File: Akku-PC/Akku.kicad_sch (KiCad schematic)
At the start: 59 parts, among them J1 Conn_02x10_Odd_Even, J2 Conn_01x02, J3 Conn_01x04, J4 Conn_01x02, J5 Conn_02x10_Odd_Even, J6 Conn_02x10_Odd_Even, J7 Conn_01x02, J8 Conn_01x02, SW1 Digitast, SW2 Digitast, SW3 Digitast, U1 74HC14, U2 74HC00, U4 74HC08, U5 74LS193, U6 74LS541, U7 74LS193, U8 74LS540

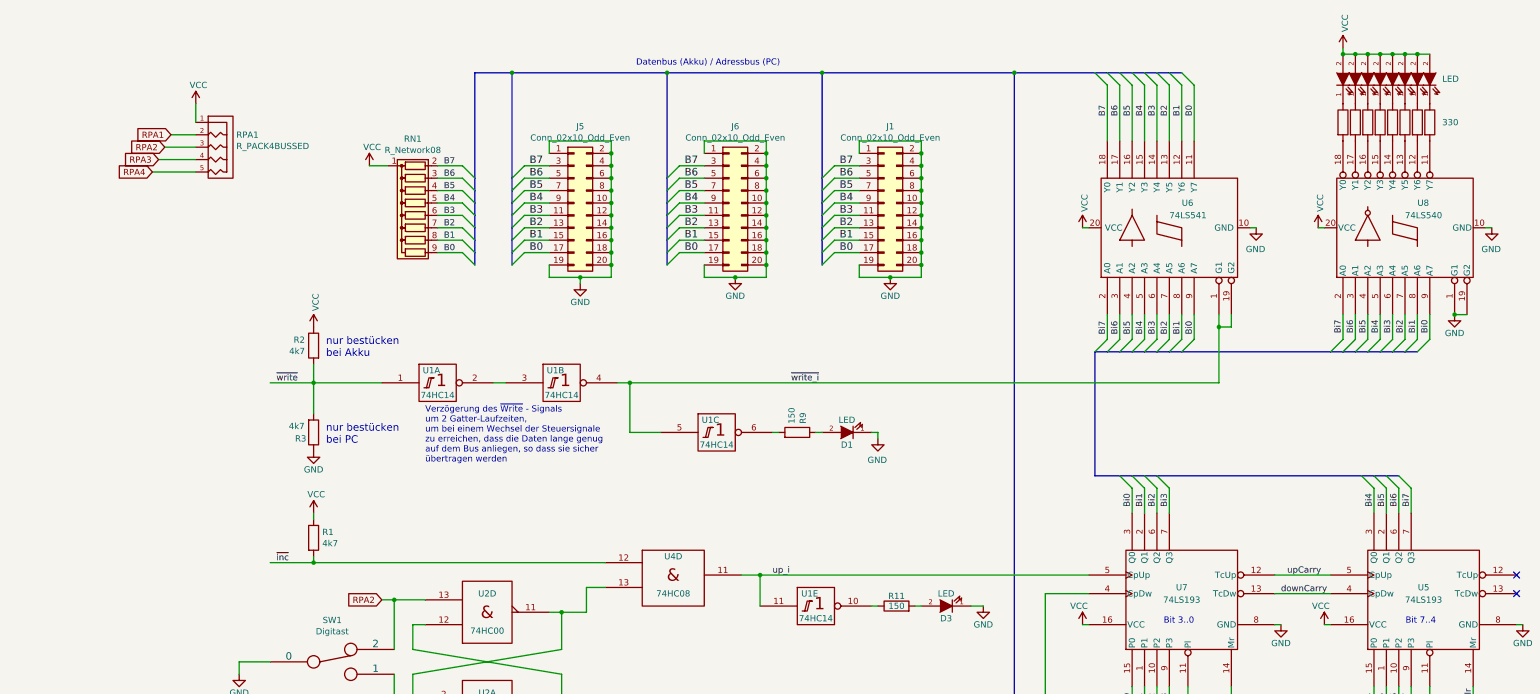
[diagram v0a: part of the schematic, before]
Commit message: - Werte von Bauteilen in den Schaltplänen ergänzt - weitere Hinweise zum Nachbau
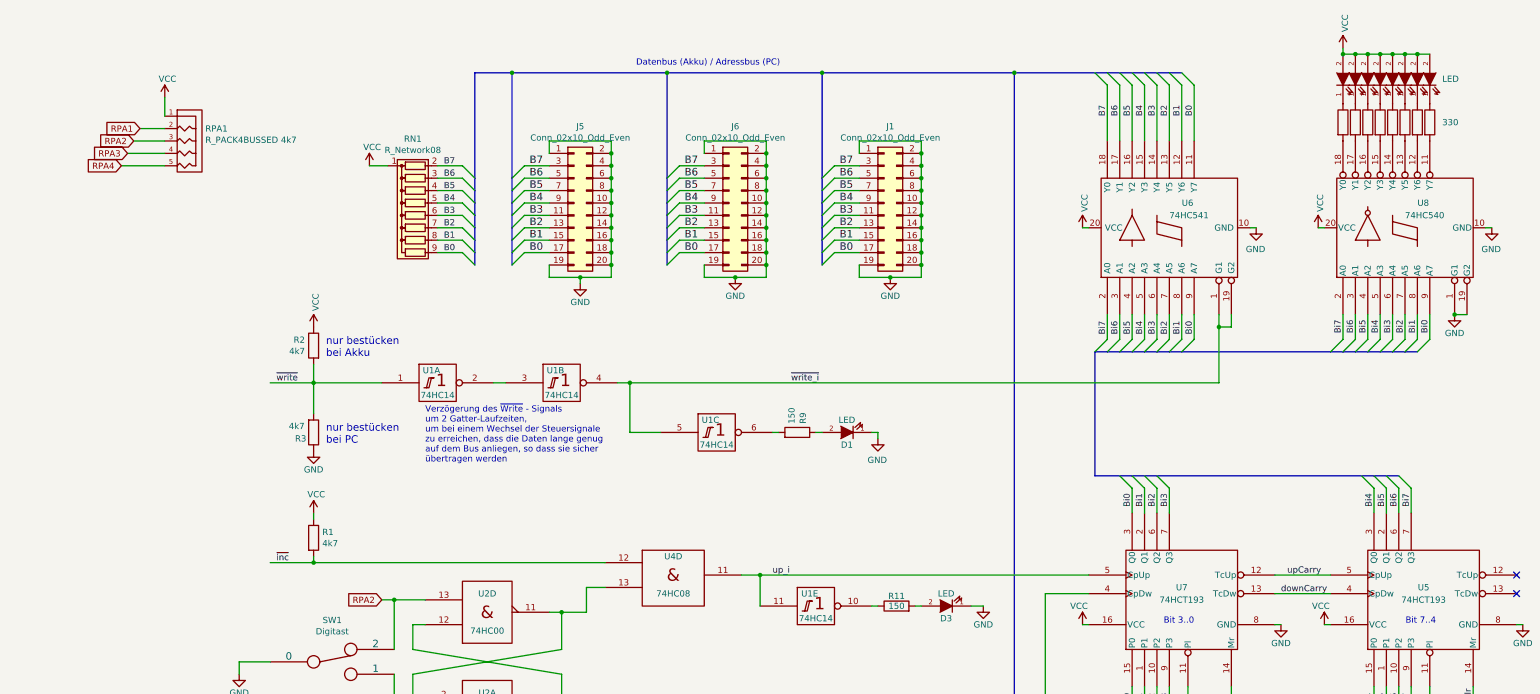
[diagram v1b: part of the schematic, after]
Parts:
- RPA1: value R_PACK4BUSSED -> R_PACK4BUSSED 4k7
- U5, U7: value 74LS193 -> 74HCT193
- U6: value 74LS541 -> 74HC541
- U8: value 74LS540 -> 74HC540
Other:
- moved on the sheet: RPA1

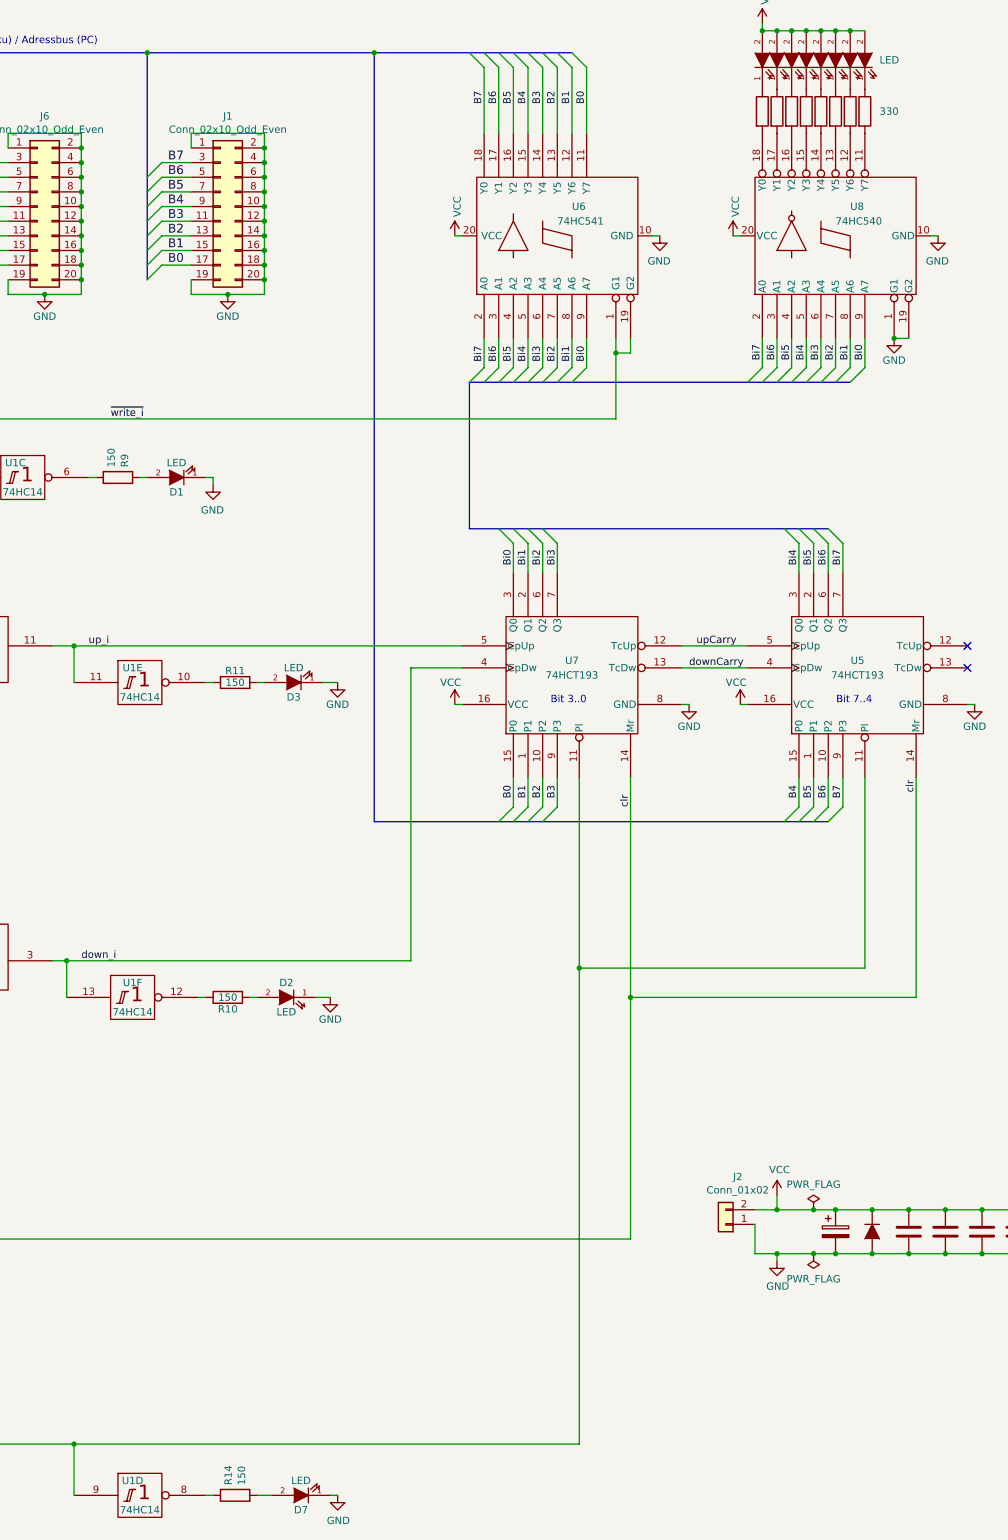
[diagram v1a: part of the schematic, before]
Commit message: Alle Vorwiderstände vor LEDs in 680 Ohm geändert (Issue 5)
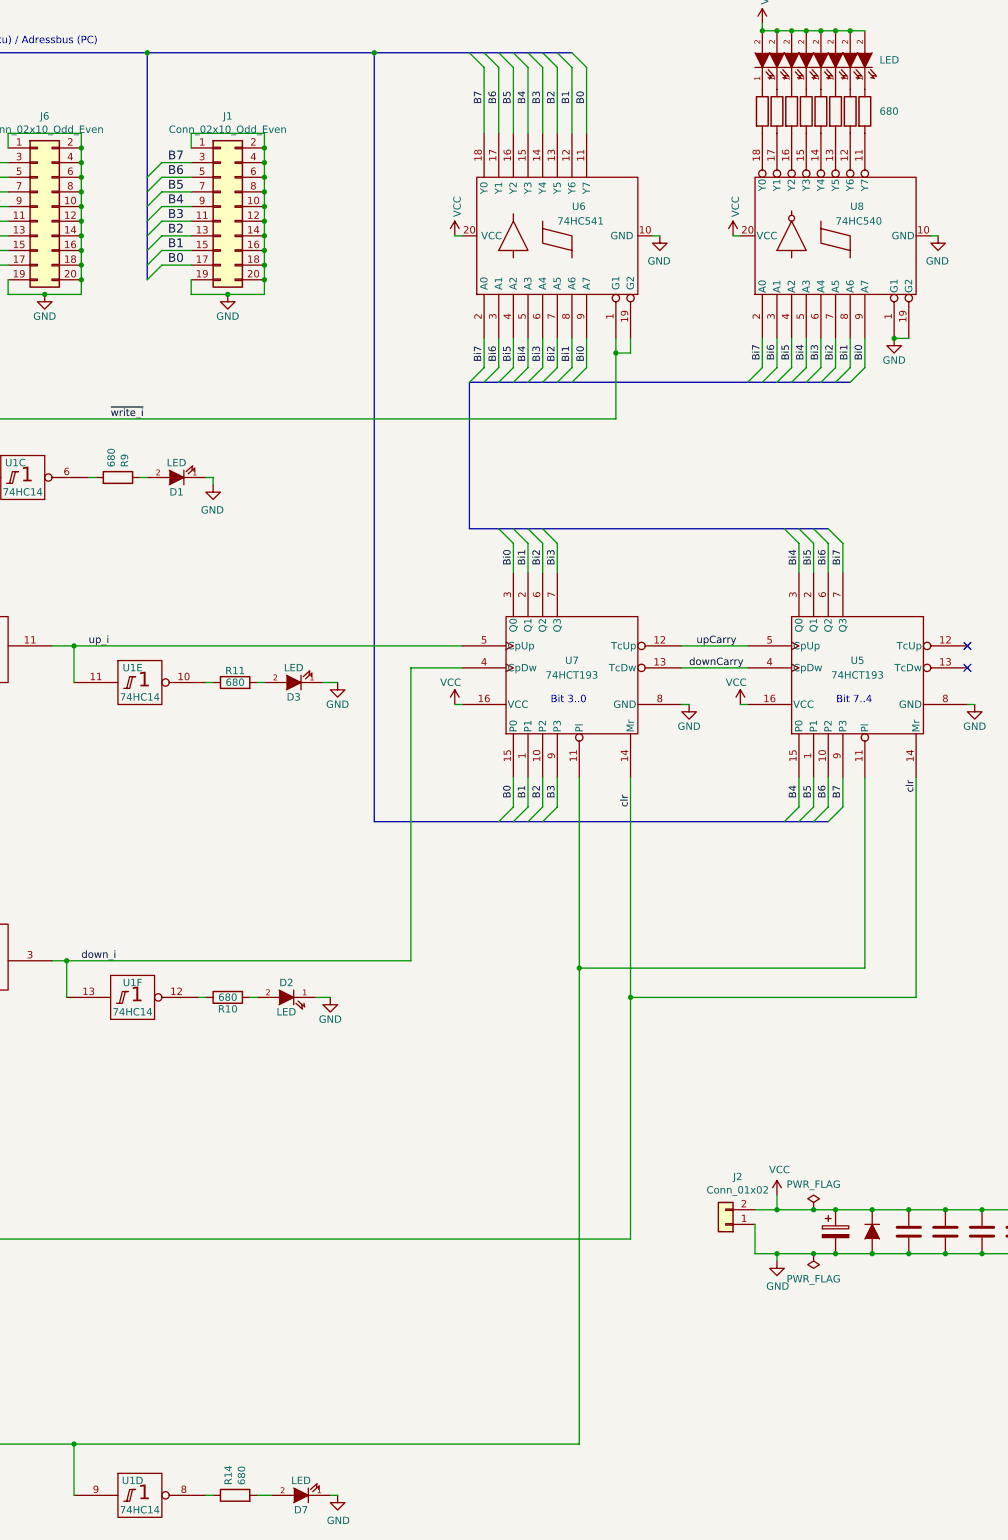
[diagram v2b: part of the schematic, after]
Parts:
- R10, R11, R14, R9: value 150 -> 680
- R13, R15, R16, R17, R18, R19, R20, R21: value 330 -> 680
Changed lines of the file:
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@@
       (effects (font (size 1.27 1.27)) (justify left) hide)
     )
-    (property "Value" "330" (at 292.608 37.973 0)
+    (property "Value" "680" (at 292.608 37.973 0)
       (effects (font (size 1.27 1.27)) (justify left) hide)
     )
@@
       (effects (font (size 1.27 1.27)) (justify left) hide)
     )
-    (property "Value" "330" (at 295.148 37.973 0)
+    (property "Value" "680" (at 295.148 37.973 0)
       (effects (font (size 1.27 1.27)) (justify left) hide)
     )
@@
       (effects (font (size 1.27 1.27)) (justify left) hide)
     )
-    (property "Value" "330" (at 297.688 37.973 0)
+    (property "Value" "680" (at 297.688 37.973 0)
       (effects (font (size 1.27 1.27)) (justify left) hide)
     )
@@
       (effects (font (size 1.27 1.27)) (justify left) hide)
     )
-    (property "Value" "330" (at 300.228 37.973 0)
+    (property "Value" "680" (at 300.228 37.973 0)
       (effects (font (size 1.27 1.27)) (justify left) hide)
     )
@@
       (effects (font (size 1.27 1.27)) (justify left) hide)
     )
-    (property "Value" "330" (at 302.768 37.973 0)
+    (property "Value" "680" (at 302.768 37.973 0)
       (effects (font (size 1.27 1.27)) (justify left) hide)
     )
@@
       (effects (font (size 1.27 1.27)) (justify left) hide)
     )
-    (property "Value" "330" (at 305.308 37.973 0)
+    (property "Value" "680" (at 305.308 37.973 0)
       (effects (font (size 1.27 1.27)) (justify left) hide)
     )
@@
       (effects (font (size 1.27 1.27)) (justify left) hide)
     )
-    (property "Value" "330" (at 307.848 37.973 0)
+    (property "Value" "680" (at 307.848 37.973 0)
       (effects (font (size 1.27 1.27)) (justify left) hide)
     )
@@
       (effects (font (size 1.27 1.27)) (justify left) hide)
     )
-    (property "Value" "330" (at 311.15 36.83 0)
+    (property "Value" "680" (at 311.15 36.83 0)
       (effects (font (size 1.27 1.27)) (justify left))
     )
@@
       (effects (font (size 1.27 1.27)) (justify left))
     )
-    (property "Value" "150" (at 200.533 275.082 0)
+    (property "Value" "680" (at 200.533 275.082 0)
       (effects (font (size 1.27 1.27)) (justify left))
     )
@@
       (effects (font (size 1.27 1.27)) (justify left))
     )
-    (property "Value" "150" (at 177.927 98.552 0)
+    (property "Value" "680" (at 177.927 98.552 0)
       (effects (font (size 1.27 1.27)) (justify left))
     )
@@
       (effects (font (size 1.27 1.27)))
     )
-    (property "Value" "150" (at 199.39 135.89 90)
+    (property "Value" "680" (at 199.39 135.89 90)
       (effects (font (size 1.27 1.27)))
     )
@@
       (effects (font (size 1.27 1.27)))
     )
-    (property "Value" "150" (at 198.12 190.5 90)
-      (effects (font (size 1.27 1.27)))
-    )
+    (property "Value" "680" (at 198.12 190.5 90)
+      (effects (font (size 1.27 1.27)))
+    )
